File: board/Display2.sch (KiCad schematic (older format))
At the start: 20 parts, among them Q15 2N7002, Q18 2N7002, Q21 2N7002, Q24 2N7002, Q25 2N7002, Q26 2N7002, Q27 2N7002, Q28 2N7002, Q29 2N7002, Q30 2N7002, Q31 2N7002, Q32 2N7002, Q33 2N7002, Q34 2N7002, Q35 2N7002, Q36 2N7002, Q37 2N7002, Q38 2N7002, Q39 2N7002, Q40 2N7002

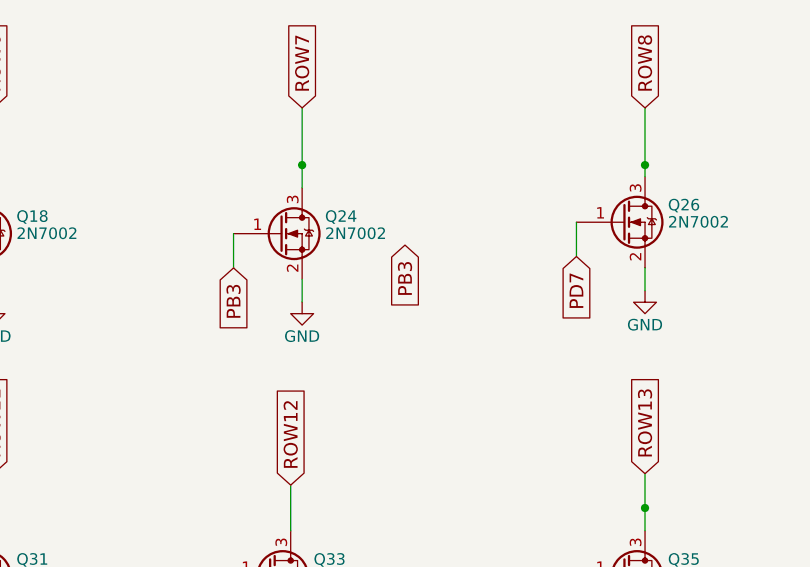
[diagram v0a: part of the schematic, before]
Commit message: Moved around components and added cutouts
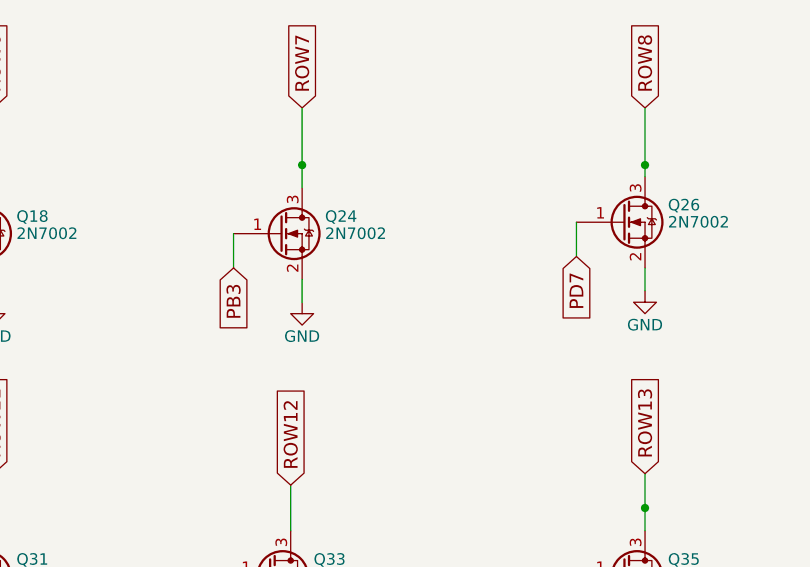
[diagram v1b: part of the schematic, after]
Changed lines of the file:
@@
 $Descr A4 11693 8268
 encoding utf-8
-Sheet 5 9
+Sheet 5 10
 Title ""
 Date ""
@@
 Text GLabel 4150 3050 3    60   Input ~ 0
 PD7
-Text GLabel 3400 3000 3    60   Input ~ 0
-PB3
 Text GLabel 1300 3100 3    60   Input ~ 0
 PB4
@@
 $EndComp
 $Comp
-L GND #PWR97
+L GND #PWR101
 U 1 1 5EA89AF4
 P 1650 1650
-F 0 "#PWR97" H 1650 1400 50  0001 C CNN
+F 0 "#PWR101" H 1650 1400 50  0001 C CNN
 F 1 "GND" H 1650 1500 50  0000 C CNN
 F 2 "" H 1650 1650 50  0001 C CNN
@@
 $EndComp
 $Comp
-L GND #PWR99
+L GND #PWR103
 U 1 1 5EA89E1B
 P 2900 1650
-F 0 "#PWR99" H 2900 1400 50  0001 C CNN
+F 0 "#PWR103" H 2900 1400 50  0001 C CNN
 F 1 "GND" H 2900 1500 50  0000 C CNN
 F 2 "" H 2900 1650 50  0001 C CNN
@@
 PB7
 $Comp
-L GND #PWR103
+L GND #PWR107
 U 1 1 5EA8A5D5
 P 4400 1650
-F 0 "#PWR103" H 4400 1400 50  0001 C CNN
+F 0 "#PWR107" H 4400 1400 50  0001 C CNN
 F 1 "GND" H 4400 1500 50  0000 C CNN
 F 2 "" H 4400 1650 50  0001 C CNN
@@
 $EndComp
 $Comp
-L GND #PWR107
+L GND #PWR111
 U 1 1 5EA8AB91
 P 5750 1650
-F 0 "#PWR107" H 5750 1400 50  0001 C CNN
+F 0 "#PWR111" H 5750 1400 50  0001 C CNN
 F 1 "GND" H 5750 1500 50  0000 C CNN
 F 2 "" H 5750 1650 50  0001 C CNN
@@
 $EndComp
 $Comp
-L GND #PWR111
+L GND #PWR115
 U 1 1 5EA8B01A
 P 7100 1700
-F 0 "#PWR111" H 7100 1450 50  0001 C CNN
+F 0 "#PWR115" H 7100 1450 50  0001 C CNN
 F 1 "GND" H 7100 1550 50  0000 C CNN
 F 2 "" H 7100 1700 50  0001 C CNN
@@
 $EndComp
 $Comp
-L GND #PWR95
+L GND #PWR99
 U 1 1 5EA8B4E3
 P 1600 3250
-F 0 "#PWR95" H 1600 3000 50  0001 C CNN
+F 0 "#PWR99" H 1600 3000 50  0001 C CNN
 F 1 "GND" H 1600 3100 50  0000 C CNN
 F 2 "" H 1600 3250 50  0001 C CNN
@@
 $EndComp
 $Comp
-L GND #PWR101
+L GND #PWR105
 U 1 1 5EA8BB55
 P 2950 3250
-F 0 "#PWR101" H 2950 3000 50  0001 C CNN
+F 0 "#PWR105" H 2950 3000 50  0001 C CNN
 F 1 "GND" H 2950 3100 50  0000 C CNN
 F 2 "" H 2950 3250 50  0001 C CNN
@@
 $EndComp
 $Comp
-L GND #PWR104
+L GND #PWR108
 U 1 1 5EA8C1F3
 P 4450 3200
-F 0 "#PWR104" H 4450 2950 50  0001 C CNN
+F 0 "#PWR108" H 4450 2950 50  0001 C CNN
 F 1 "GND" H 4450 3050 50  0000 C CNN
 F 2 "" H 4450 3200 50  0001 C CNN
@@
 $EndComp
 $Comp
-L GND #PWR108
+L GND #PWR112
 U 1 1 5EA8C647
 P 5800 3250
-F 0 "#PWR108" H 5800 3000 50  0001 C CNN
+F 0 "#PWR112" H 5800 3000 50  0001 C CNN
 F 1 "GND" H 5800 3100 50  0000 C CNN
 F 2 "" H 5800 3250 50  0001 C CNN
@@
 $EndComp
 $Comp
-L GND #PWR112
+L GND #PWR116
 U 1 1 5EA8CFA9
 P 7150 3250
-F 0 "#PWR112" H 7150 3000 50  0001 C CNN
+F 0 "#PWR116" H 7150 3000 50  0001 C CNN
 F 1 "GND" H 7150 3100 50  0000 C CNN
 F 2 "" H 7150 3250 50  0001 C CNN
@@
 $EndComp
 $Comp
-L GND #PWR96
+L GND #PWR100
 U 1 1 5EA8D59A
 P 1600 4750
-F 0 "#PWR96" H 1600 4500 50  0001 C CNN
+F 0 "#PWR100" H 1600 4500 50  0001 C CNN
 F 1 "GND" H 1600 4600 50  0000 C CNN
 F 2 "" H 1600 4750 50  0001 C CNN
@@
 $EndComp
 $Comp
-L GND #PWR100
+L GND #PWR104
 U 1 1 5EA8F065
 P 2900 4750
-F 0 "#PWR100" H 2900 4500 50  0001 C CNN
+F 0 "#PWR104" H 2900 4500 50  0001 C CNN
 F 1 "GND" H 2900 4600 50  0000 C CNN
 F 2 "" H 2900 4750 50  0001 C CNN
@@
 $EndComp
 $Comp
-L GND #PWR105
+L GND #PWR109
 U 1 1 5EA8F9B9
 P 4450 4750
-F 0 "#PWR105" H 4450 4500 50  0001 C CNN
+F 0 "#PWR109" H 4450 4500 50  0001 C CNN
 F 1 "GND" H 4450 4600 50  0000 C CNN
 F 2 "" H 4450 4750 50  0001 C CNN
@@
 $EndComp
 $Comp
-L GND #PWR109
+L GND #PWR113
 U 1 1 5EA9007B
 P 5800 4700
-F 0 "#PWR109" H 5800 4450 50  0001 C CNN
+F 0 "#PWR113" H 5800 4450 50  0001 C CNN
 F 1 "GND" H 5800 4550 50  0000 C CNN
 F 2 "" H 5800 4700 50  0001 C CNN
@@
 $EndComp
 $Comp
-L GND #PWR113
+L GND #PWR117
 U 1 1 5EA90602
 P 7150 4700
-F 0 "#PWR113" H 7150 4450 50  0001 C CNN
+F 0 "#PWR117" H 7150 4450 50  0001 C CNN
 F 1 "GND" H 7150 4550 50  0000 C CNN
 F 2 "" H 7150 4700 50  0001 C CNN
@@
 $EndComp
 $Comp
-L GND #PWR98
+L GND #PWR102
 U 1 1 5EA90FE2
 P 1650 6250
-F 0 "#PWR98" H 1650 6000 50  0001 C CNN
+F 0 "#PWR102" H 1650 6000 50  0001 C CNN
 F 1 "GND" H 1650 6100 50  0000 C CNN
 F 2 "" H 1650 6250 50  0001 C CNN
@@
 $EndComp
 $Comp
-L GND #PWR102
+L GND #PWR106
 U 1 1 5EA914F6
 P 3000 6250
-F 0 "#PWR102" H 3000 6000 50  0001 C CNN
+F 0 "#PWR106" H 3000 6000 50  0001 C CNN
 F 1 "GND" H 3000 6100 50  0000 C CNN
 F 2 "" H 3000 6250 50  0001 C CNN
@@
 $EndComp
 $Comp
-L GND #PWR106
+L GND #PWR110
 U 1 1 5EA91A63
 P 4500 6300
-F 0 "#PWR106" H 4500 6050 50  0001 C CNN
+F 0 "#PWR110" H 4500 6050 50  0001 C CNN
 F 1 "GND" H 4500 6150 50  0000 C CNN
 F 2 "" H 4500 6300 50  0001 C CNN
@@
 $EndComp
 $Comp
-L GND #PWR110
+L GND #PWR114
 U 1 1 5EA9204F
 P 5850 6350
-F 0 "#PWR110" H 5850 6100 50  0001 C CNN
+F 0 "#PWR114" H 5850 6100 50  0001 C CNN
 F 1 "GND" H 5850 6200 50  0000 C CNN
 F 2 "" H 5850 6350 50  0001 C CNN
@@
 $EndComp
 $Comp
-L GND #PWR114
+L GND #PWR118
 U 1 1 5EA925E6
 P 7200 6250
-F 0 "#PWR114" H 7200 6000 50  0001 C CNN
+F 0 "#PWR118" H 7200 6000 50  0001 C CNN
 F 1 "GND" H 7200 6100 50  0000 C CNN
 F 2 "" H 7200 6250 50  0001 C CNN
